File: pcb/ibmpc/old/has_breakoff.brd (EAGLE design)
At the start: 123 x 64.6 mm, 34 parts, among them J2 ATX24RH

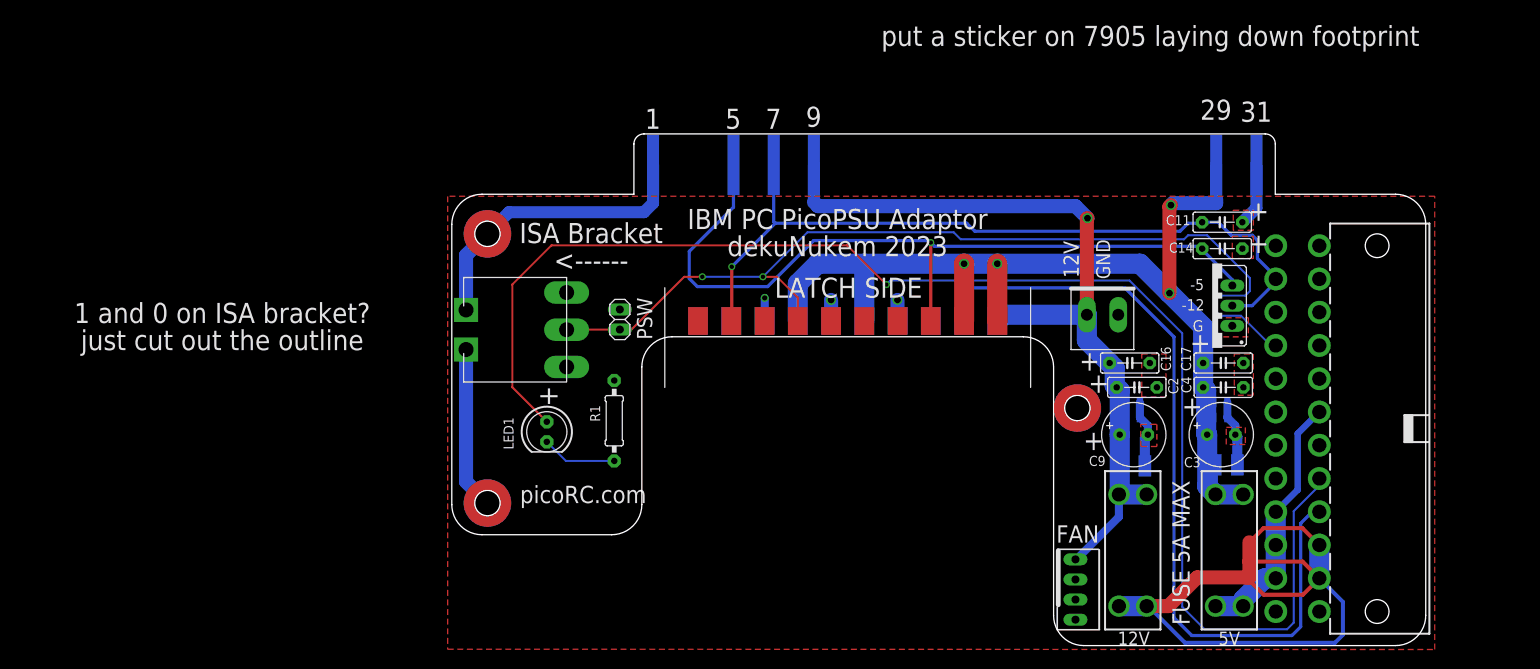
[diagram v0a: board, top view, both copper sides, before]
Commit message: added fingers for 5V and 12V, minor adjustments
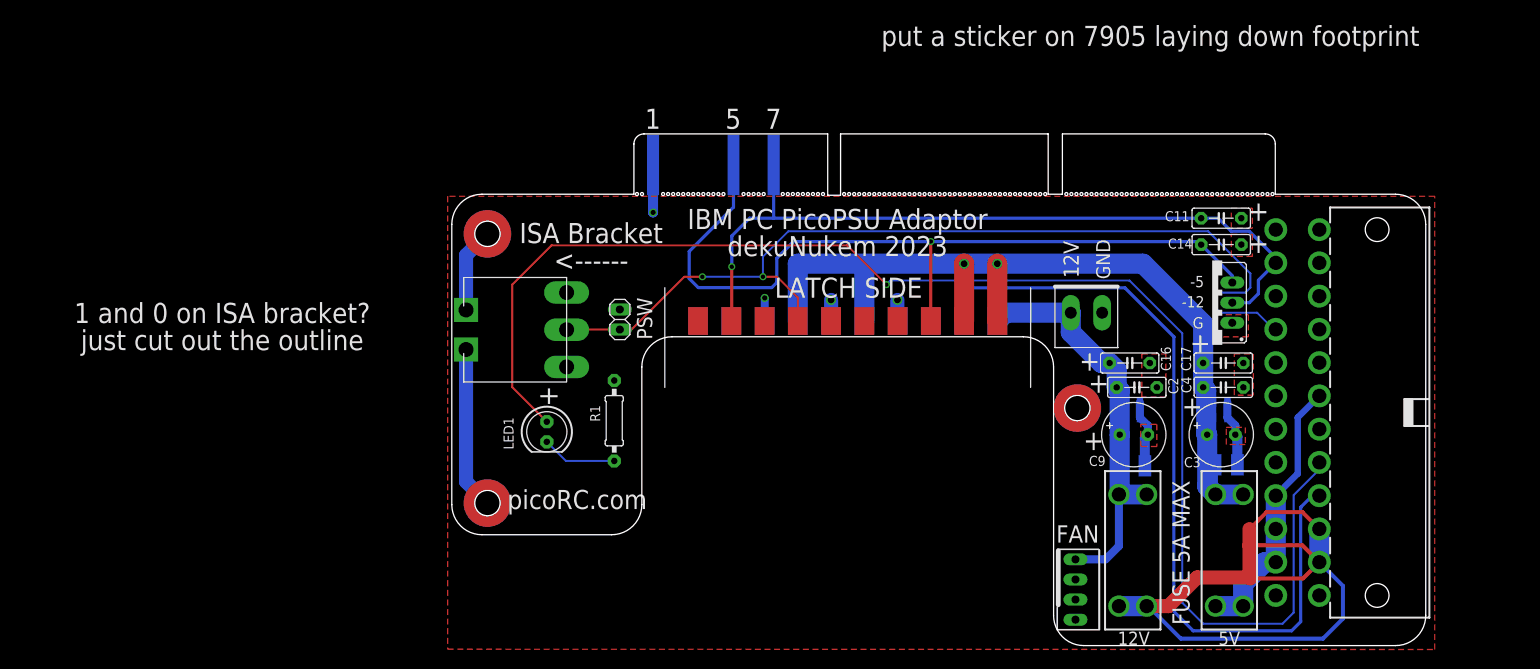
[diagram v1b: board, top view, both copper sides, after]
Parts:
- removed U$13, U$15, U$16: ISA, blade:ISAPAD
- moved U$3 2.05 mm to (81.2, 42.0)
- moved J2 2.03 mm to (115.3, 29.4)
- moved C11 0.52 mm to (98.2, 54.0)
- moved C14 0.52 mm to (98.2, 50.6)
- moved IC1 0.38 mm to (97.0, 43.3)
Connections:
- net +12V: no longer U$13.P$1
- net +5V: no longer U$16.P$1
- net GND: no longer U$15.P$1
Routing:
- net +12V: track 113.3 -> 62.9 mm, vias 1 -> 0
- net GND: track 91.8 -> 62.5 mm, vias 3 -> 4
- net +5V: track 137.2 -> 117.0 mm, vias 4 -> 2
- net N$6: track 32.8 -> 34.9 mm
- net -5V: track 100.8 -> 102.6 mm
- net N$8: track 93.3 -> 94.2 mm
- net N$5: track 101.5 -> 102.2 mm
- net -12V: track 97.8 -> 98.4 mm
- net N$3: track 120.1 -> 120.6 mm
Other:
- outline, holes or cut-outs redrawn
- board text removed: "+12V"
- board text removed: "+5V"
- board text removed: "-12V"
- board text removed: "-5V"
- board text removed: "29"
- board text removed: "31"
- board text removed: "9"
